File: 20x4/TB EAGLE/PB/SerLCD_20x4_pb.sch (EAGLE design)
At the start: 20 parts, among them J1 AVR_PROG, J3 SER_LCD20X4, U1 5V Flying Jalapeno, U2 74LVC4066_MUX_1:1_X4

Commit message: 20x4 pb routing done
-changed switch to isolate FJ SPI lines (because the new pi_grammer has isolation built in)
-added more support beam standoffs
-moved to new FJ footprint for easier assembly on RA 2x30 header.
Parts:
- removed JP1: MISO, SparkFun-Jumpers:JUMPER-SMT_2_NC_PASTE_NO-SILK
- removed JP2: SCK, SparkFun-Jumpers:JUMPER-SMT_2_NC_PASTE_NO-SILK
- removed JP3: RST, SparkFun-Jumpers:JUMPER-SMT_2_NC_PASTE_NO-SILK
- removed JP4: MOSI, SparkFun-Jumpers:JUMPER-SMT_2_NC_PASTE_NO-SILK
- added C1: 0.1uF, Testing:CAP0603-CAP
- U1: device Testing:FLYING_JALAPENO_V2MALE -> Testing:FLYING_JALAPENO_V3MALE
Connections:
- net PGM_SWITCH_EN renamed SPI_FJ_SWITCH_EN
- removed net MISO_P: J1.1, JP1.1, U2.1Y
- removed net MOSI_P: J1.4, JP4.1, U2.4Y
- removed net RST_P: J1.5, JP3.1, U2.3Y
- removed net SCK_P: J1.3, JP2.1, U2.2Y
- new net CS_FJ: U1.53(SS), U2.3Y
- new net MISO_FJ: U1.50(MISO), U2.1Y
- new net MOSI_FJ: U1.51(MOSI), U2.4Y
- new net SCK_FJ: U1.52(SCK), U2.2Y
- net 5V_VIN: now also C1.1
- net CS: now also U2.3Z; no longer U1.53(SS)
- net GND: now also C1.2
- net MISO: now also J1.1; no longer JP1.2, U1.50(MISO)
- net MOSI: now also J1.4; no longer JP4.2, U1.51(MOSI)
- net RST: now also J1.5; no longer JP3.2, U2.3Z
- net RX1_FJ: no longer J3.TXO
- net SCK: now also J1.3; no longer JP2.2, U1.52(SCK)
- net TX1_FJ: no longer J3.RX@19, J3.RXI
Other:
- note removed: "Bypass switch jumpers"
- moved on the sheet: J1

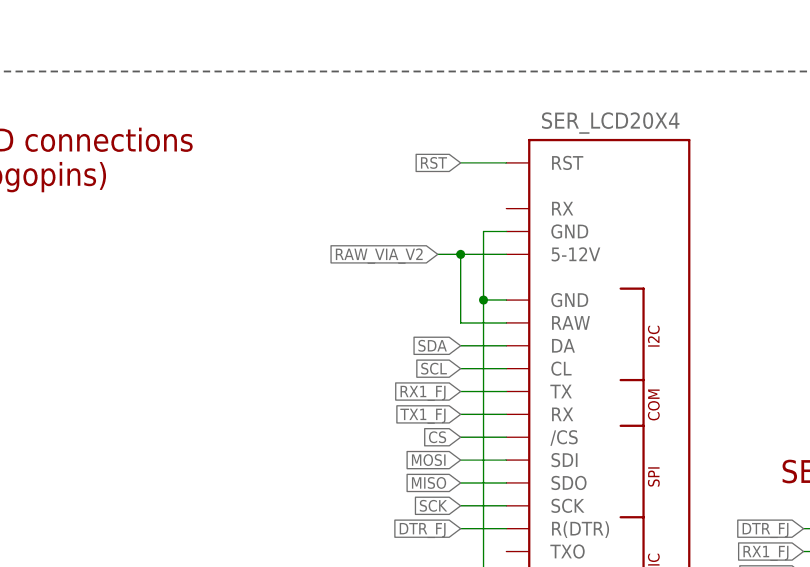
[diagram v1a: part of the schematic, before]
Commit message: 20x4 testbed PB updated for new qwiic connector version
-also removed old PM footprints, cuz these aren't used in making acrylic layers anyways, and they are now out of date with pogopin spacing.
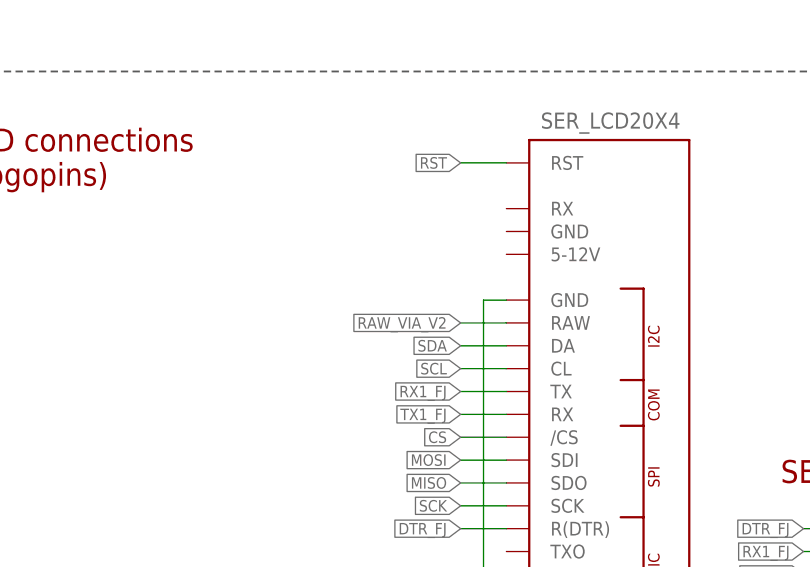
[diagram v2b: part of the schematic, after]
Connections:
- net GND: no longer J3.GND@18
- net RAW_VIA_V2: no longer J3.5-12V
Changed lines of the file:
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@@
 <?xml version="1.0" encoding="utf-8"?>
 <!DOCTYPE eagle SYSTEM "eagle.dtd">
-<eagle version="9.2.2">
+<eagle version="9.5.2">
 <drawing>
 <settings>
@@
 <wire x1="177.8" y1="50.8" x2="175.26" y2="50.8" width="0.1524" layer="91"/>
 <junction x="175.26" y="50.8"/>
-<pinref part="J3" gate="G$1" pin="GND@18"/>
-<wire x1="177.8" y1="93.98" x2="175.26" y2="93.98" width="0.1524" layer="91"/>
-<wire x1="175.26" y1="93.98" x2="175.26" y2="86.36" width="0.1524" layer="91"/>
-<junction x="175.26" y="86.36"/>
 <pinref part="GND5" gate="1" pin="GND"/>
 </segment>
@@
 </segment>
 <segment>
-<pinref part="J3" gate="G$1" pin="5-12V"/>
-<wire x1="177.8" y1="91.44" x2="172.72" y2="91.44" width="0.1524" layer="91"/>
-<label x="170.18" y="91.44" size="1.27" layer="95" rot="R180" xref="yes"/>
+<label x="172.72" y="83.82" size="1.27" layer="95" rot="R180" xref="yes"/>
 <pinref part="J3" gate="G$1" pin="RAW"/>
-<wire x1="172.72" y1="91.44" x2="170.18" y2="91.44" width="0.1524" layer="91"/>
 <wire x1="177.8" y1="83.82" x2="172.72" y2="83.82" width="0.1524" layer="91"/>
-<wire x1="172.72" y1="83.82" x2="172.72" y2="91.44" width="0.1524" layer="91"/>
-<junction x="172.72" y="91.44"/>
-</segment>
-</net>
+</segment>
+</net>
